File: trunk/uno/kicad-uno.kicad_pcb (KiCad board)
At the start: 2 copper layers, 68.6 x 53.3 mm, 48 parts, among them J1 RESET_EN, Q1 FDN340P, SW1 RESET, U1 NCP1117 5V, U2 LP2985-33DBVR, U3 ATMEGA16U2-MU(R), U5 LM358, X2 USB-MINI-AB

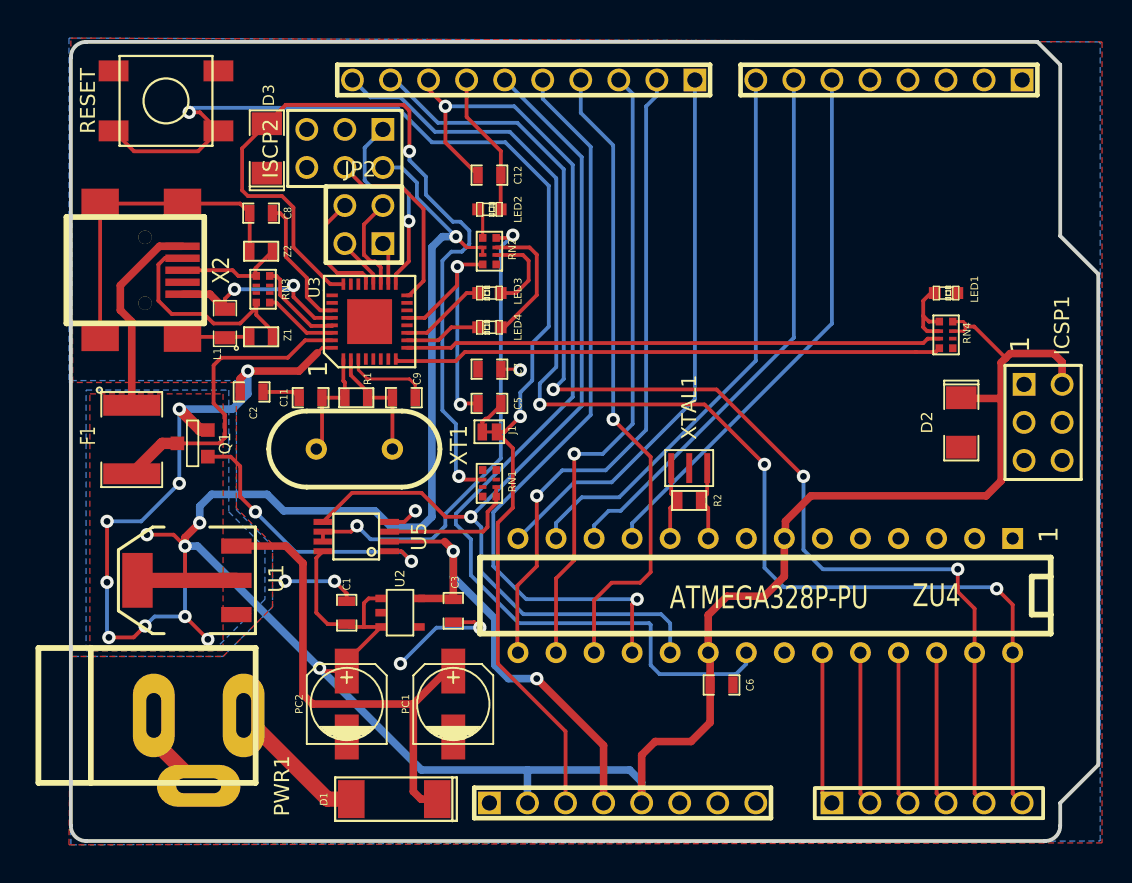
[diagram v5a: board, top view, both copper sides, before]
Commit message: Routing complete. Board complete.
Just need to do the 3D packages for the resistor arrays and rsonator.

Oh -- the previous revisions had the wrong size resistor array parts. That
was corrected in this version. (SM0402, apparently.)
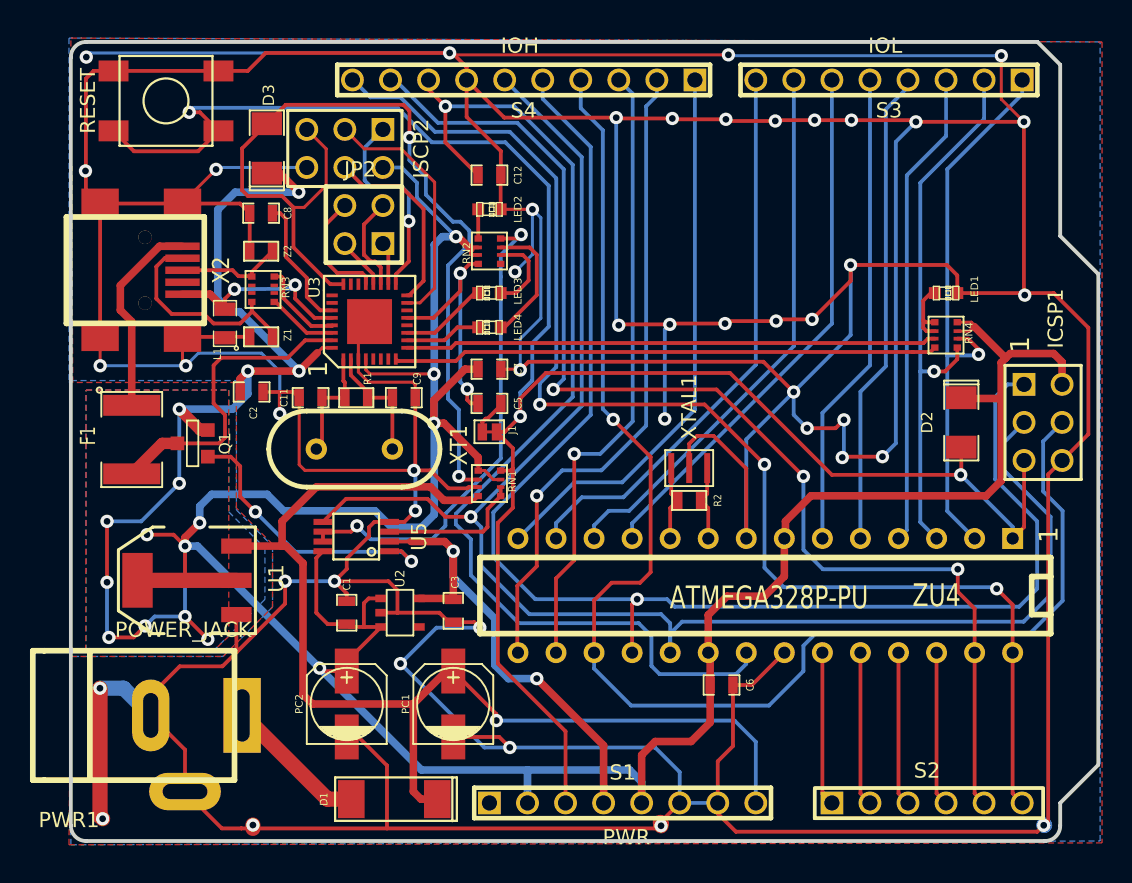
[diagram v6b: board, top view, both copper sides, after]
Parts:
- PWR1: footprint BARREL_JACK -> JACK_NEB21R
- RN1, RN2, RN3, RN4: footprint RN_EXB-28V -> RN0402_EXB-2HV
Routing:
- net GND: track 66.6 -> 628.2 mm, vias 6 -> 45
- net N-000001: track 42.8 -> 93.1 mm
- net /RESET: track 86.0 -> 134.1 mm, vias 2 -> 3
- net N-000002: track 50.7 -> 94.0 mm
- net VIN: track 32.5 -> 75.2 mm, vias 0 -> 1
- net SCK: track 65.7 -> 106.3 mm
- net +5V: track 231.7 -> 270.8 mm, vias 14 -> 18
- net /IO0: track 0.00 -> 37.6 mm, vias 0 -> 1
- net /IO1: track 0.00 -> 36.6 mm, vias 0 -> 1
- net /IO4: track 0.00 -> 31.9 mm
- net /IO3: track 0.00 -> 31.9 mm
- net /IO2: track 0.00 -> 31.9 mm
- net /USB/SCK2: track 0.00 -> 16.8 mm
- net /USB/RESET2: track 55.9 -> 61.9 mm
- net DTR: track 17.8 -> 16.5 mm
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
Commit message: Board fully completed v1.0.
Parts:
- added JP1: Solder Bridge, JSOLD, B.Cu at (38.2, 39.9)
- added REF: VAL**, POWER_POLARITY_REF, B.Cu at (29.5, 71.9)
- S1: footprint pin_array_8x1 -> pin_array_6x1
- U3: footprint QFN32 -> QFN32_2x2-SINK
- moved PWR1 2.75 mm to (33.0, 71.9)
- moved S1 2.54 mm to (64.8, 76.2)
- moved C12 1.55 mm to (51.8, 34.0)
- renumbered X2 to USB1, XTAL1 to X1, ZU4 to ZU1
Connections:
- S1 pad 1: (no net) -> /RESET
- S1 pad 2: +5V -> +3V3
- S1 pad 3: /RESET -> +5V
- S1 pad 4: +3V3 -> GND
- S1 pad 5: +5V -> GND
- S1 pad 6: GND -> VIN
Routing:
- net GND: track 628.2 -> 635.2 mm, vias 45 -> 46
- net N-0000039: track 9.60 -> 7.07 mm
- net +5V: track 270.8 -> 268.6 mm
- net N-0000074: track 12.9 -> 14.5 mm
- net AREF: track 72.2 -> 71.3 mm
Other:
- board text added: "+"
- board text added: "-"
- board text added: "-10"
- board text added: "-11"
- board text added: "-3"
- board text added: "-5"
- board text added: "-6"
- board text added: "-9"
- board text added: "0"
- board text added: "12"
- board text added: "13"
- board text added: "2"
- board text added: "3"
- board text added: "3V3"
- board text added: "4"
- board text added: "5"
- board text added: "5V"
- board text added: "7"
- board text added: "7-12VDC"
- board text added: "8"
- board text added: "ANALOG IN"
- board text added: "AREF"
- board text added: "DIGITAL (-PWM)"
- board text added: "GND"
- board text added: "Kicaduino v1.0"
- board text added: "POWER"
- board text added: "RESET"
- board text added: "RX<-0"
- board text added: "SCL"
- board text added: "SDA"
- board text added: "TX->1"
- board text added: "Vin"
- board text added: "http://kicaduino.googlecode.com"

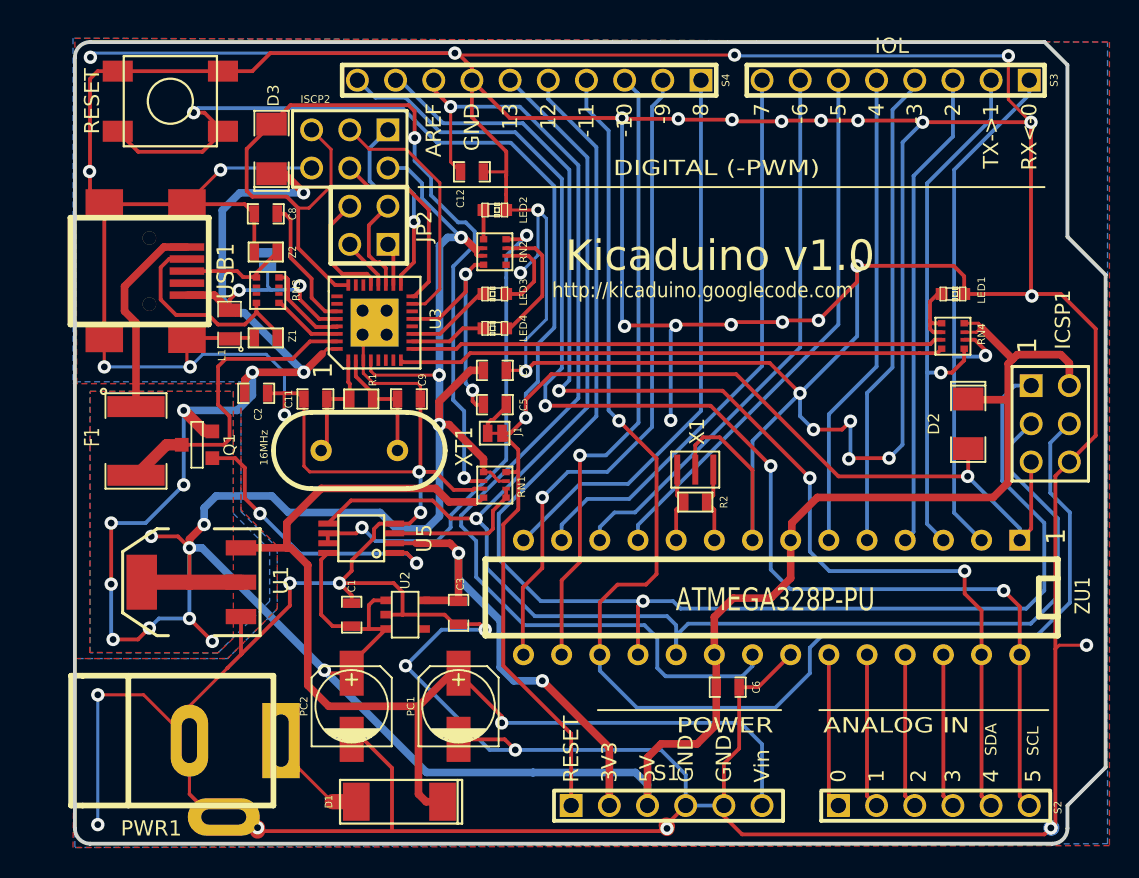
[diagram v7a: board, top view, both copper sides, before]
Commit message: Mounting holes added. Had to move the power jack out a bit.
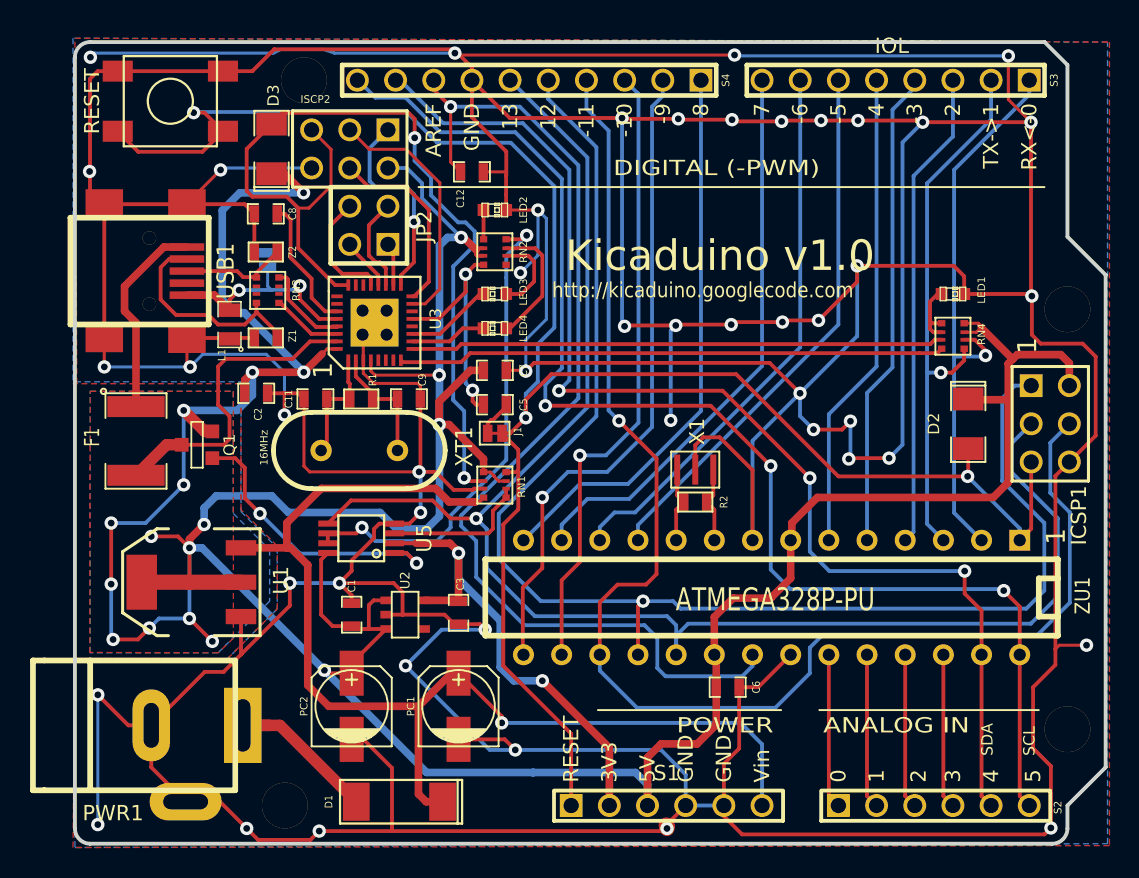
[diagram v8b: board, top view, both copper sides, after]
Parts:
- added HOLE_130x130mil: VAL**, HOLE_120x120mil, F.Cu at (39.4, 76.2)
- added HOLE_130x130mil: VAL**, HOLE_120x120mil, F.Cu at (91.4, 71.1)
- added HOLE_130x130mil: VAL**, HOLE_120x120mil, F.Cu at (91.4, 43.2)
- added HOLE_130x250mil: VAL**, HOLE_120x120mil, F.Cu at (40.6, 27.9)
- moved PWR1 2.74 mm to (30.5, 70.9)
- moved REF 1.85 mm to (27.7, 71.4)
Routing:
- net N-0000039: track 7.07 -> 9.90 mm
- net GND: track 635.2 -> 637.4 mm, vias 46 -> 47
- net /USB/RESET2: track 61.9 -> 61.2 mm
